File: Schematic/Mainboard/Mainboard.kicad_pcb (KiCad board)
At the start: 2 copper layers, 70 x 70 mm, 18 parts, among them J1 Motor_A, J2 Motor_B, J3 Motor_C, J4 BATT_IN, J5 Servo, J6 Servo, J7 ESC, J8 ESC_PWR, SW1 MAIN_CUTOFF, U1 ESP32-LOLIN32-Lite, U4 RFM69HW, U5 XL60019_Boost_Module, U6 Mini360

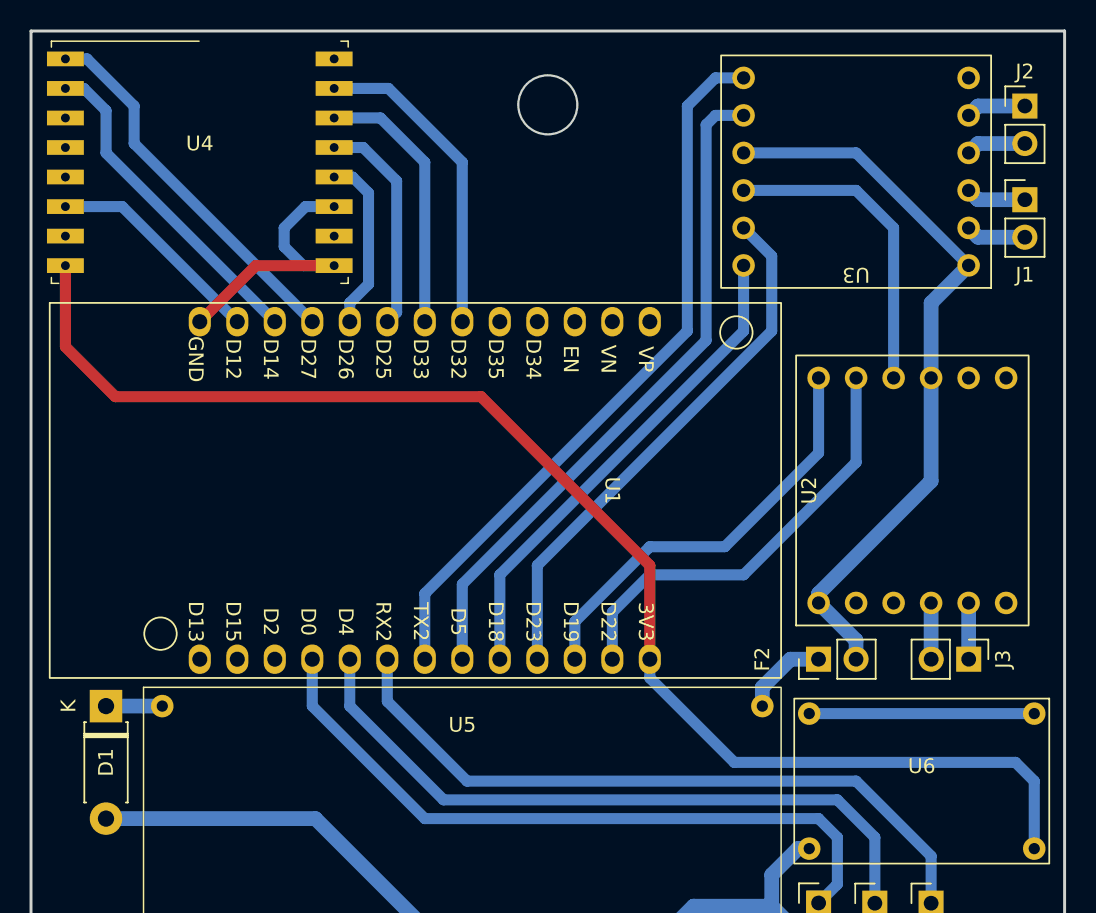
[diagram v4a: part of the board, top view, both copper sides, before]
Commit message: rework radio class
telemetry packets now come as part of the ACK, so there is less chance of both transmitters stepping on  each  other.
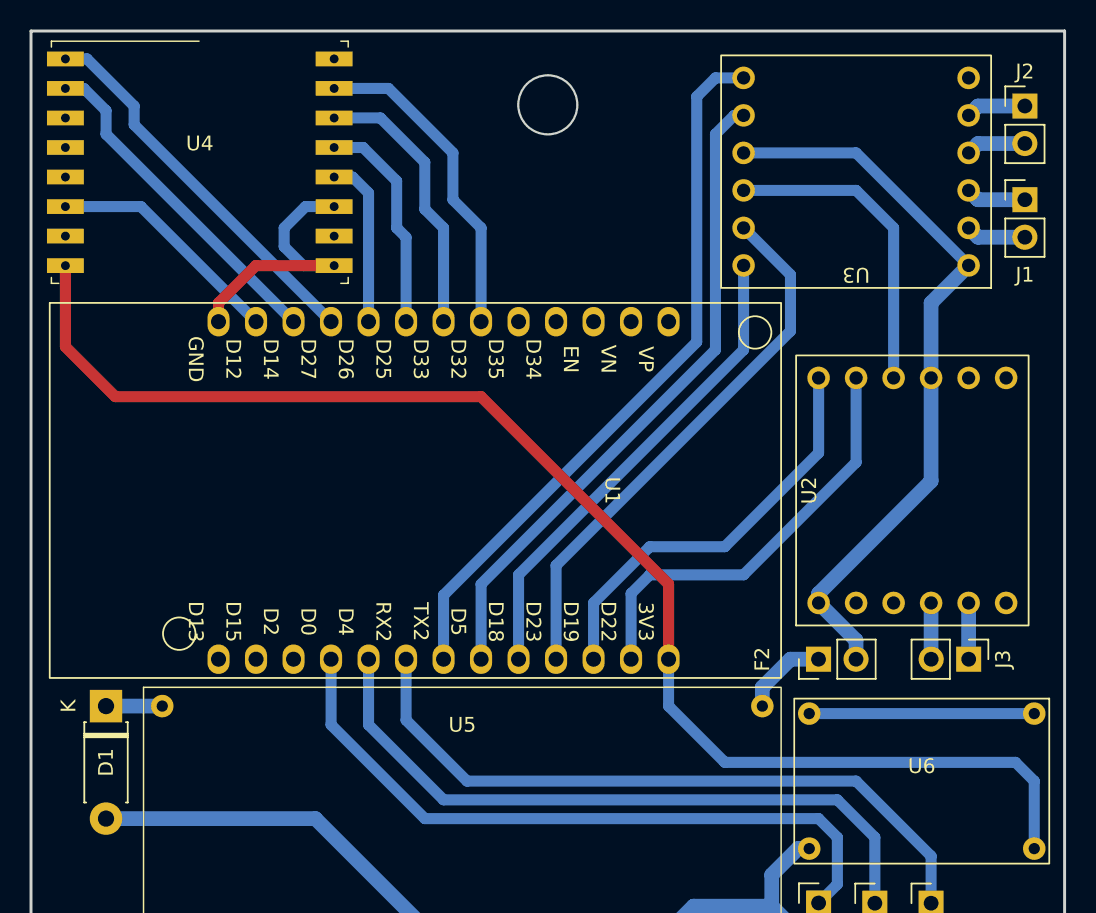
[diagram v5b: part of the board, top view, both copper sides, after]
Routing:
- net /M A2: track 45.8 -> 44.6 mm
- net /AUX: track 14.9 -> 16.1 mm
- net /M C2: track 28.9 -> 28.3 mm
- net /SERVO 1: track 47.4 -> 46.9 mm
- net /NSS: track 21.5 -> 22.1 mm
- net /MOSI: track 18.2 -> 18.7 mm
- net /M B1: track 36.6 -> 37.1 mm
- net /M A1: track 49.4 -> 48.9 mm
- net /INTER: track 22.4 -> 22.9 mm
- net /RESET: track 25.6 -> 26.1 mm
- net /M C1: track 29.6 -> 29.1 mm
- net GND: track 81.3 -> 80.8 mm
- net /ESC: track 47.2 -> 46.7 mm
- net /SERVO 2: track 46.9 -> 46.4 mm
- net /M B2: track 33.5 -> 33.0 mm
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
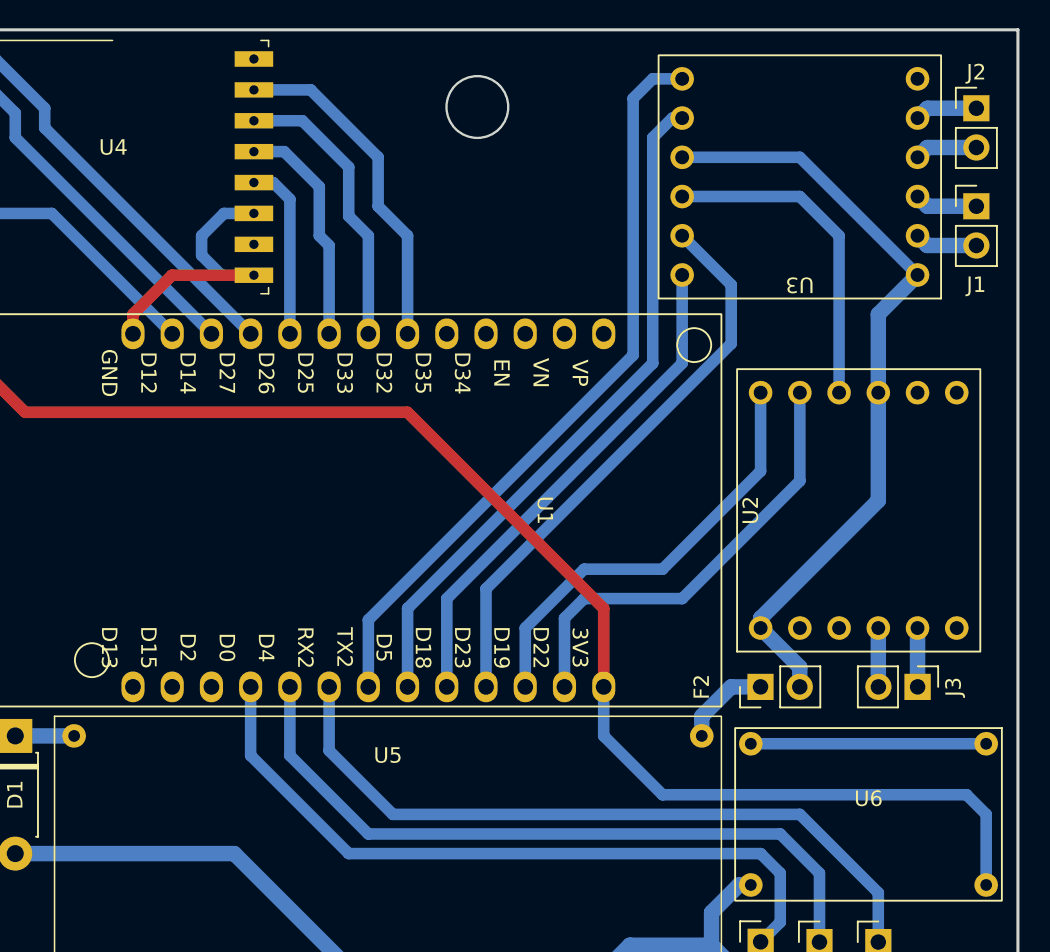
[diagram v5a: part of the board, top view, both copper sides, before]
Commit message: set up radio module on ESP32
also worked on getting the ESP32 debugger up and running
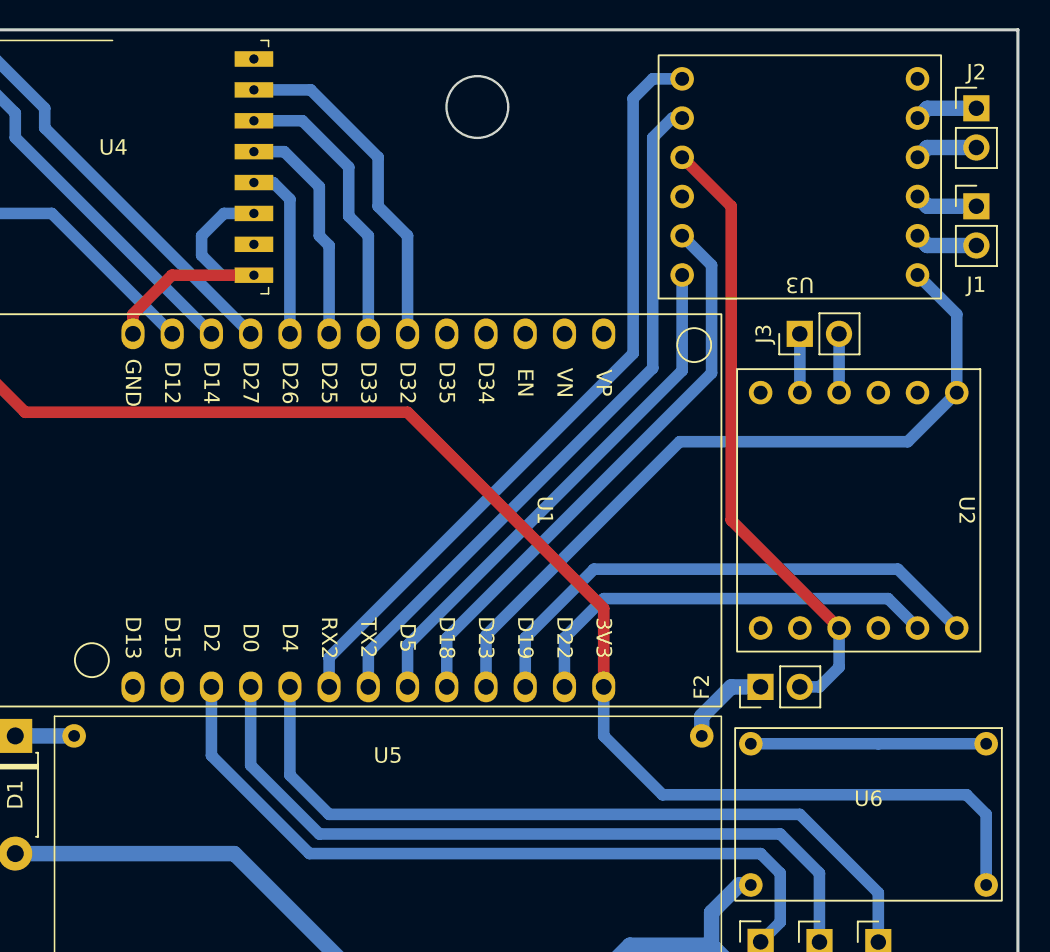
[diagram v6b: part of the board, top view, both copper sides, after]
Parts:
- moved J3 24.1 mm to (184.1, 97.2), turned to 90 degrees
- moved U2 2.54 mm to (189.2, 108.6), turned to -90 degrees
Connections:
- F2 pad 2: +12V -> +10V
- U1 pad 22: unconnected-(U1-D2-Pad22) -> /SERVO 1
- U1 pad 23: /SERVO 1 -> /SERVO 2
- U1 pad 24: /SERVO 2 -> /ESC
- U1 pad 25: /ESC -> /M A1
- U1 pad 27: /M A1 -> /M A2
- U1 pad 34: /M A2 -> /M B2
- U1 pad 35: /M B2 -> /M B1
- U1 pad 36: /M B1 -> /SLEEP
- U2 pad 1: +12V -> /SLEEP
- U2 pad 9: +12V -> +10V
- U3 pad 1: +12V -> /SLEEP
- U3 pad 9: +12V -> +10V
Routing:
- net +12V: track 50.3 -> 0.00 mm
- net /SLEEP: track 0.00 -> 49.0 mm
- net +10V: track 0.00 -> 40.3 mm
- net GND: track 80.8 -> 59.4 mm
- net /M C2: track 28.3 -> 34.5 mm
- net /ESC: track 46.7 -> 50.2 mm
- net /SERVO 2: track 46.4 -> 49.3 mm
- net /SERVO 1: track 46.9 -> 49.4 mm
- net /M C1: track 29.1 -> 27.9 mm
- net /M A1: track 48.9 -> 50.0 mm
- net /M B2: track 33.0 -> 34.0 mm
- net /M A2: track 44.6 -> 45.6 mm

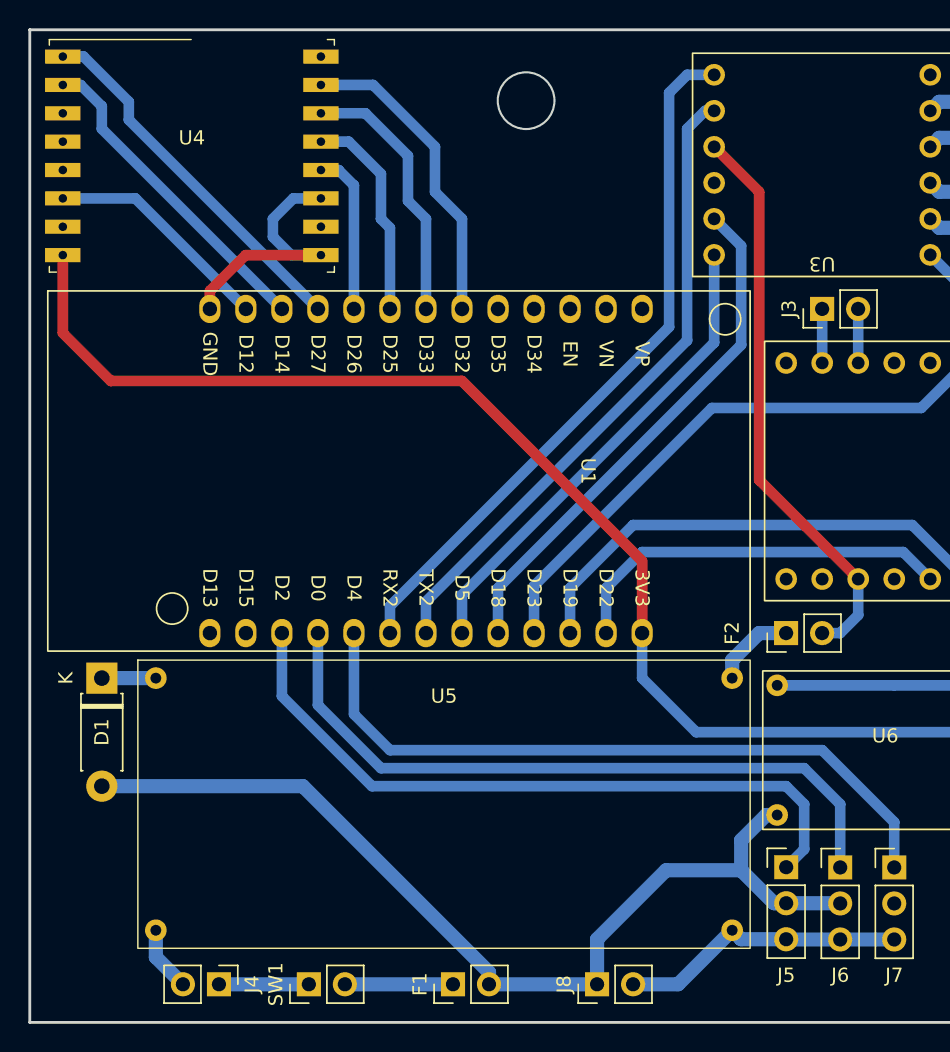
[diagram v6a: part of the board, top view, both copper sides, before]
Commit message: Work on weight reduction
thin the shell in order to get the total weight under 1 lb.
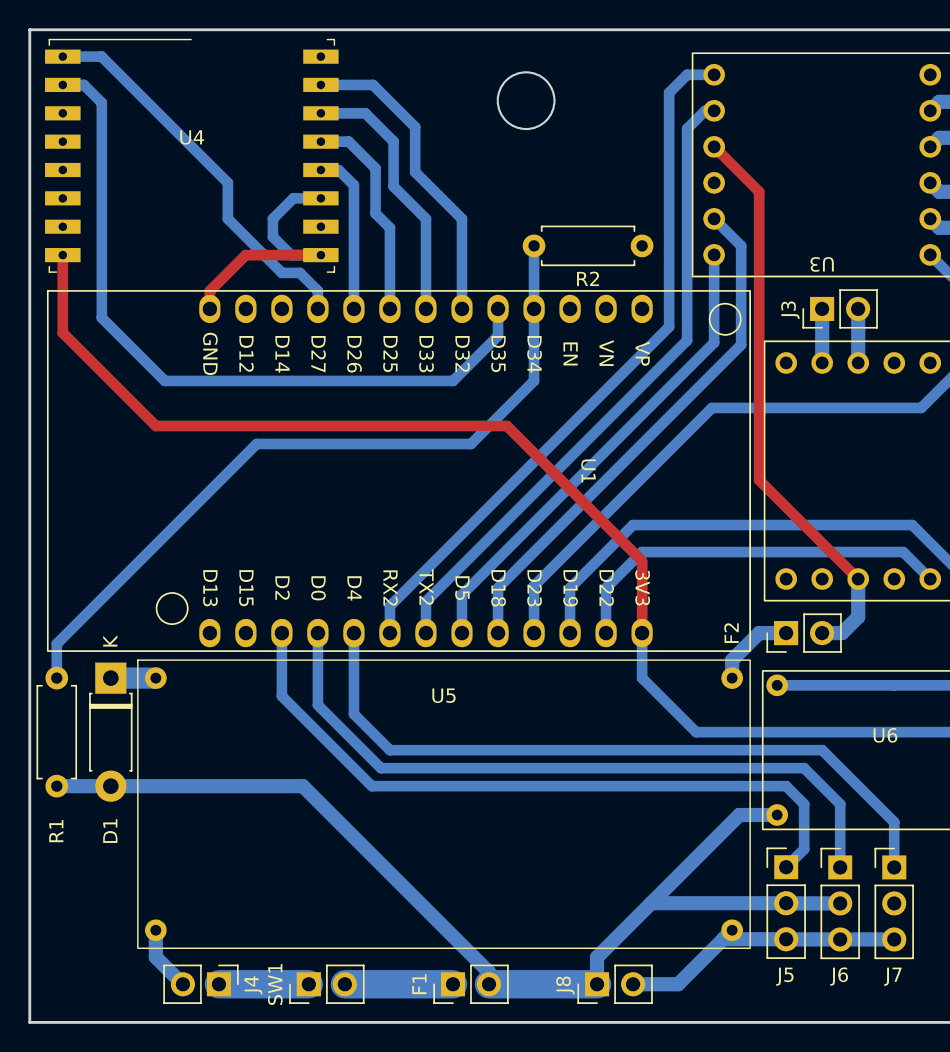
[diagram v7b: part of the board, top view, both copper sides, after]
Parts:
- added R1: 150k Ohm, Resistor_THT:R_Axial_DIN0207_L6.3mm_D2.5mm_P7.62mm_Horizontal, F.Cu at (130.2, 123.2)
- added R2: 10k Ohm, Resistor_THT:R_Axial_DIN0207_L6.3mm_D2.5mm_P7.62mm_Horizontal, F.Cu at (171.4, 92.7)
- moved D1 0.64 mm to (134.0, 123.2)
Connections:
- U1 pad 10: unconnected-(U1-D34-Pad10) -> /BAT READ
- U1 pad 11: unconnected-(U1-D35-Pad11) -> /INTER
- U1 pad 17: /INTER -> /TMS
- U1 pad 18: /AUX -> /TDI
- U1 pad 20: unconnected-(U1-D13-Pad20) -> /TCK
- U1 pad 21: unconnected-(U1-D15-Pad21) -> /TDO
- U4 pad 6: /AUX -> unconnected-(U4-DIO4-Pad6)
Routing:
- net /BAT READ: track 0.00 -> 53.3 mm
- net /INTER: track 22.9 -> 51.4 mm
- net /AUX: track 16.1 -> 0.00 mm
- net /+BATT SW: track 69.9 -> 76.5 mm
- net /RESET: track 26.1 -> 27.6 mm
- net GND: track 59.4 -> 60.7 mm
- net Net-(D1-K): track 3.81 -> 3.17 mm

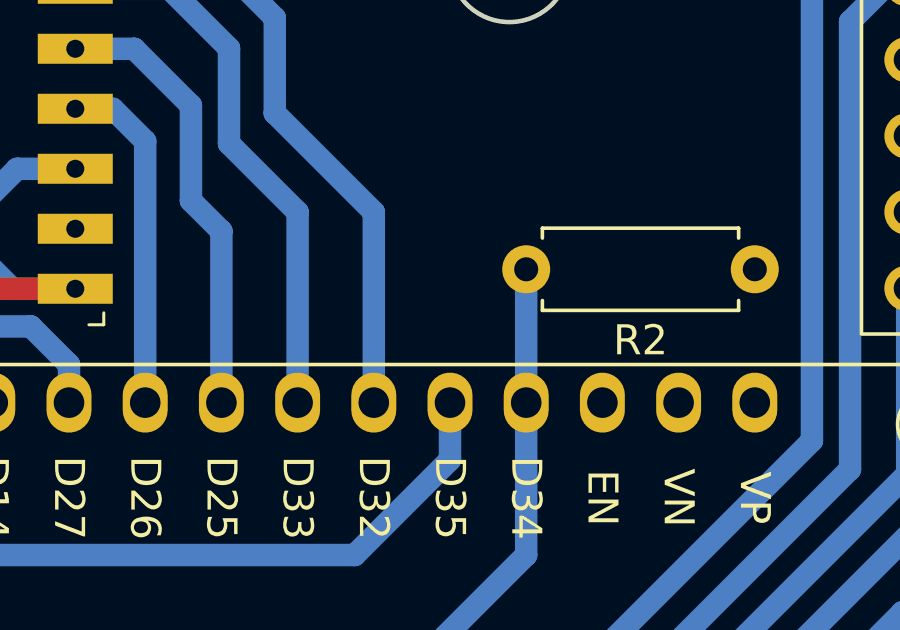
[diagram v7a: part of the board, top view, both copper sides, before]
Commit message: prepare to mill PCB
also add more sub-functions to firmware
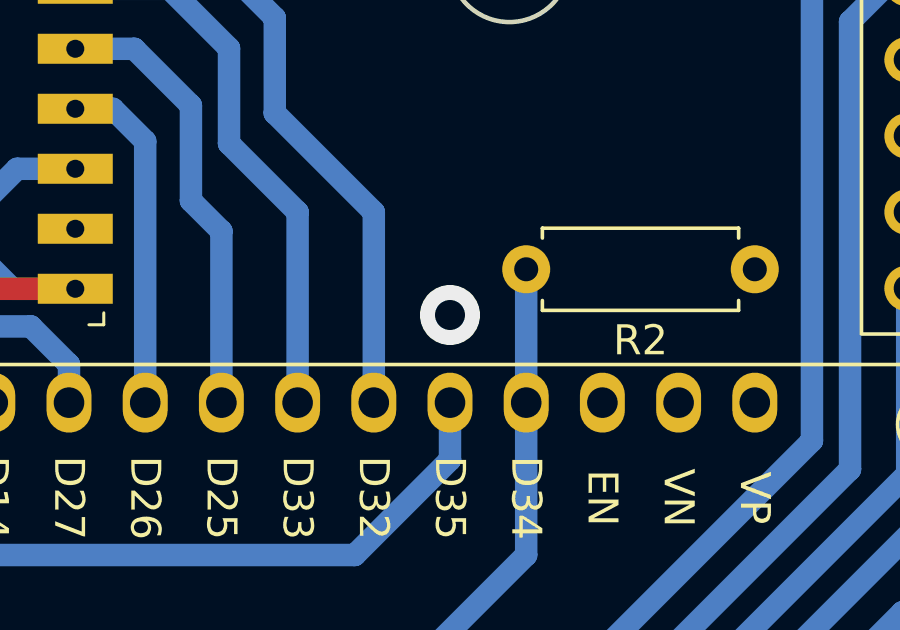
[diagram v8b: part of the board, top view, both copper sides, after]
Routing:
- net GND: vias 0 -> 1
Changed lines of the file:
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@@
   (segment (start 140.97 95.885) (end 140.97 97.155) (width 0.75) (layer "F.Cu") (net 5))
   (segment (start 148.8 93.36) (end 143.495 93.36) (width 0.75) (layer "F.Cu") (net 5))
+  (via (at 161.29 94.234) (size 2) (drill 1) (layers "F.Cu" "B.Cu") (free) (net 5))
   (segment (start 137.16 140.97) (end 137.16 142.87) (width 1) (layer "B.Cu") (net 5))
   (segment (start 148.8 93.36) (end 146.7 93.36) (width 0.75) (layer "B.Cu") (net 5))
